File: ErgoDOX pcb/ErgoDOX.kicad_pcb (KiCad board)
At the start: 2 copper layers, 182.8 x 158.9 mm, 110 parts, among them J1 USB_RH, J10 USB VCC, J11 USB_LH, J2 3.5mm, J3 JMP, J4 JMP, J5 BT_JMP, J6 EN_JMP, J7 PROG, J8 JTAG, J9 USB GND, SW0:10 SW0:3, SW0:11 SW0:2, SW0:12 SW0:1, SW0:7 SW0:6, SW0:8 SW0:5, SW0:9 SW0:4, SW1:10 SW1:3, SW1:11 SW1:2, SW1:12 SW1:1, SW1:13 SW1:0, SW1:9 SW1:4, SW2:10 SW2:3, SW2:11 SW2:2, SW2:12 SW2:1, SW2:13 SW2:0, SW2:7 SW2:6, SW2:8 SW2:5, SW2:9 SW2:4, SW3:10 SW3:3, SW3:11 SW3:2, SW3:12 SW3:1, SW3:13 SW3:0, SW3:8 SW3:5, SW3:9 SW3:4, SW4:10 SW4:3, SW4:11 SW4:2, SW4:12 SW4:1, SW4:13 SW4:0, SW4:7 SW4:6, SW4:8 SW4:5, SW4:9 SW4:4, SW5:10 SW5:3, SW5:11 SW5:2, SW5:12 SW5:1, SW5:13 SW5:0, SW5:7 SW5:6, SW5:8 SW5:5, SW5:9 SW5:4, U1 LM337_SOT223, U2 ESP32-S3 LH, U3 ESP32-S3 RH, U4 LM337_SOT223

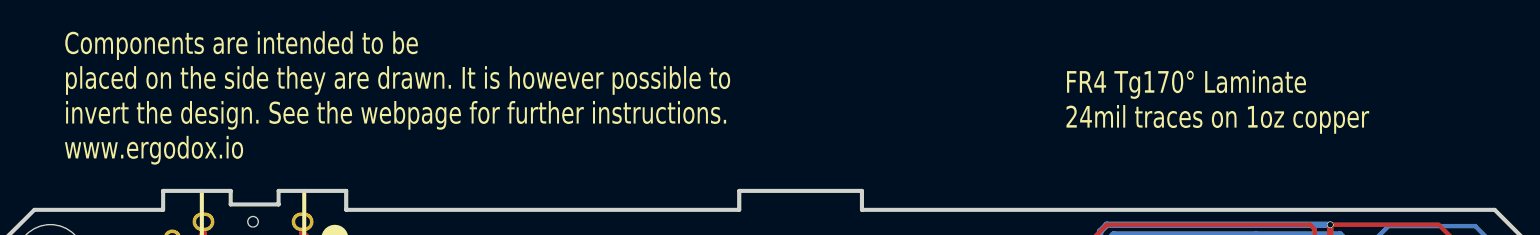
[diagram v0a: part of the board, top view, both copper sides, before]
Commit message: Remove unused silkscreen
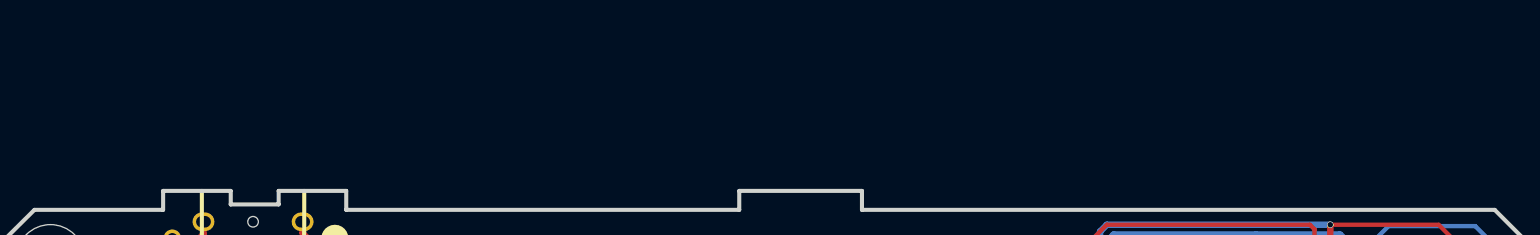
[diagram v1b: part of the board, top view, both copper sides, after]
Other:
- board text removed: "Components are intended to be placed on the side they are drawn. It is however possible to invert the design. See the webpage for further instructions. www.ergodox.io"
- board text removed: "FR4 Tg170° Laminate 24mil traces on 1oz copper"
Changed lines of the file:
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@@
     (effects (font (size 1 1) (thickness 0.15)) (justify mirror))
-  )
-  (gr_text "FR4 Tg170° Laminate\n24mil traces on 1oz copper " (at 234.188 21.463) (layer "B.SilkS")
-    (effects (font (size 2.032 1.524) (thickness 0.3048)) (justify left mirror))
   )
   (gr_text "oheaDox" (at 154.432 51.816) (layer "B.SilkS")
@@
     (effects (font (size 0.5 0.5) (thickness 0.075)) (justify mirror))
   )
-  (gr_text "オヘアドックス" (at 129.921 52.578) (layer "B.SilkS")
-    (effects (font (size 3.81 2.8575) (thickness 0.5715)) (justify mirror))
-  )
   (gr_text "RESET" (at 106.426 50.927) (layer "B.SilkS")
     (effects (font (size 1 1) (thickness 0.15)) (justify mirror))
@@
     (effects (font (size 0.75 0.75) (thickness 0.1125)))
   )
-  (gr_text "Components are intended to be\nplaced on the side they are drawn. It is however possible to\ninvert the design. See the webpage for further instructions.\nwww.ergodox.io" (at 68.58 21.59) (layer "F.SilkS")
-    (effects (font (size 2.032 1.524) (thickness 0.3048)) (justify left))
-  )
   (gr_text "GND_JMP" (at 120.777 35.179) (layer "F.SilkS")
     (effects (font (size 0.5 0.5) (thickness 0.075)))
@@
     (effects (font (size 0.5 0.5) (thickness 0.075)))
   )
-  (gr_text "FR4 Tg170° Laminate\n24mil traces on 1oz copper " (at 162.433 21.971) (layer "F.SilkS")
-    (effects (font (size 2.032 1.524) (thickness 0.3048)) (justify left))
-  )
   (gr_text "0.1uF" (at 95.885 49.022 90) (layer "F.SilkS")
